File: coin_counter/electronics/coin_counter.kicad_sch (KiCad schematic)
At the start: 51 parts, among them J1 Q_EMT, J10 H_EMT, J11 Power In, J12 Q_BTN, J13 D_BTN, J14 N_BTN, J15 P_BTN, J16 UP_BTN, J17 DN_BTN, J18 VFD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

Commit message: fixed errors
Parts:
- removed R1, R2, R3, R4, R5, R6: 220 Ohm, Resistor_THT:R_Axial_DIN0204_L3.6mm_D1.6mm_P5.08mm_Vertical, symbol Device:R_US
- removed Sensor1: Mom, Connector_JST:JST_XH_B6B-XH-A_1x06_P2.50mm_Vertical, symbol Connector_Generic:Conn_02x03_Top_Bottom
- added R10, R11, R12, R7, R8, R9: 10k, Resistor_SMD:R_0201_0603Metric, symbol Device:R_US
- added Sensor2: Mom, Connector_JST:JST_XH_B6B-XH-A_1x06_P2.50mm_Vertical, symbol Connector_Generic:Conn_02x03_Top_Bottom
- C1, C2, C3: footprint Capacitor_THT:CP_Radial_D10.0mm_P5.00mm -> Capacitor_SMD:CP_Elec_5x5.9
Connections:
- net at A1.29 (GND), A1.4 (GND), H5.1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: no longer J11.1 (Pin_1), J22.1 (Pin_1)
- net at J15.1 (Pin_1): now also U1.3 (QD)
- net at J15.2 (Pin_2): now also R10.2; no longer U2.14 (D3)
- net at C1.2, C2.2, H10.1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: now also U2.5 (D6), U2.6 (D7), Sensor2.2 (Pin_2); no longer J12.3 (Pin_3), J13.3 (Pin_3), J14.3 (Pin_3), J15.3 (Pin_3), J16.3 (Pin_3), J17.3 (Pin_3)
- net at J19.2 (Pin_2), U2.1 (~{PL}): now also Sensor2.4 (Pin_4)
- net at U2.10 (DS): now also Sensor2.3 (Pin_3)
- net at U2.11 (D0): now also R7.1; no longer J12.2 (Pin_2)
- net at U2.12 (D1): now also R8.1; no longer J13.2 (Pin_2)
- net at U2.13 (D2): now also R9.1; no longer J14.2 (Pin_2)
- net at J19.4 (Pin_4), U2.15 (~{CE}): now also Sensor2.6 (Pin_6)
- net at C1.1, C2.1, J21.2 (Pin_2)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: now also J12.3 (Pin_3), J13.3 (Pin_3), J14.3 (Pin_3), J15.3 (Pin_3), J16.3 (Pin_3), J17.3 (Pin_3), Sensor2.1 (Pin_1)
- net at J19.3 (Pin_3), U2.2 (CP): now also Sensor2.5 (Pin_5)
- net at U2.3 (D4): now also R11.1; no longer J16.2 (Pin_2)
- net at U2.4 (D5): now also R12.1; no longer J17.2 (Pin_2)
- net at J5.3 (Pin_3): now also U3.9 (Q7); no longer U3.7 (~{Q7})
- net at U1.1 (QB): now also J13.1 (Pin_1)
- net at U1.15 (QA): now also J12.1 (Pin_1)
- net at U1.2 (QC): now also J14.1 (Pin_1)
- net at U1.4 (QE): now also J16.1 (Pin_1)
- net at U1.5 (QF): now also J17.1 (Pin_1)
- new net: J12.2 (Pin_2), R7.2
- new net: R10.1, U2.14 (D3)
- new net: J17.2 (Pin_2), R12.2
- new net: J16.2 (Pin_2), R11.2
- new net: J11.1 (Pin_1), J22.1 (Pin_1)
- new net: J13.2 (Pin_2), R8.2
- new net: J14.2 (Pin_2), R9.2

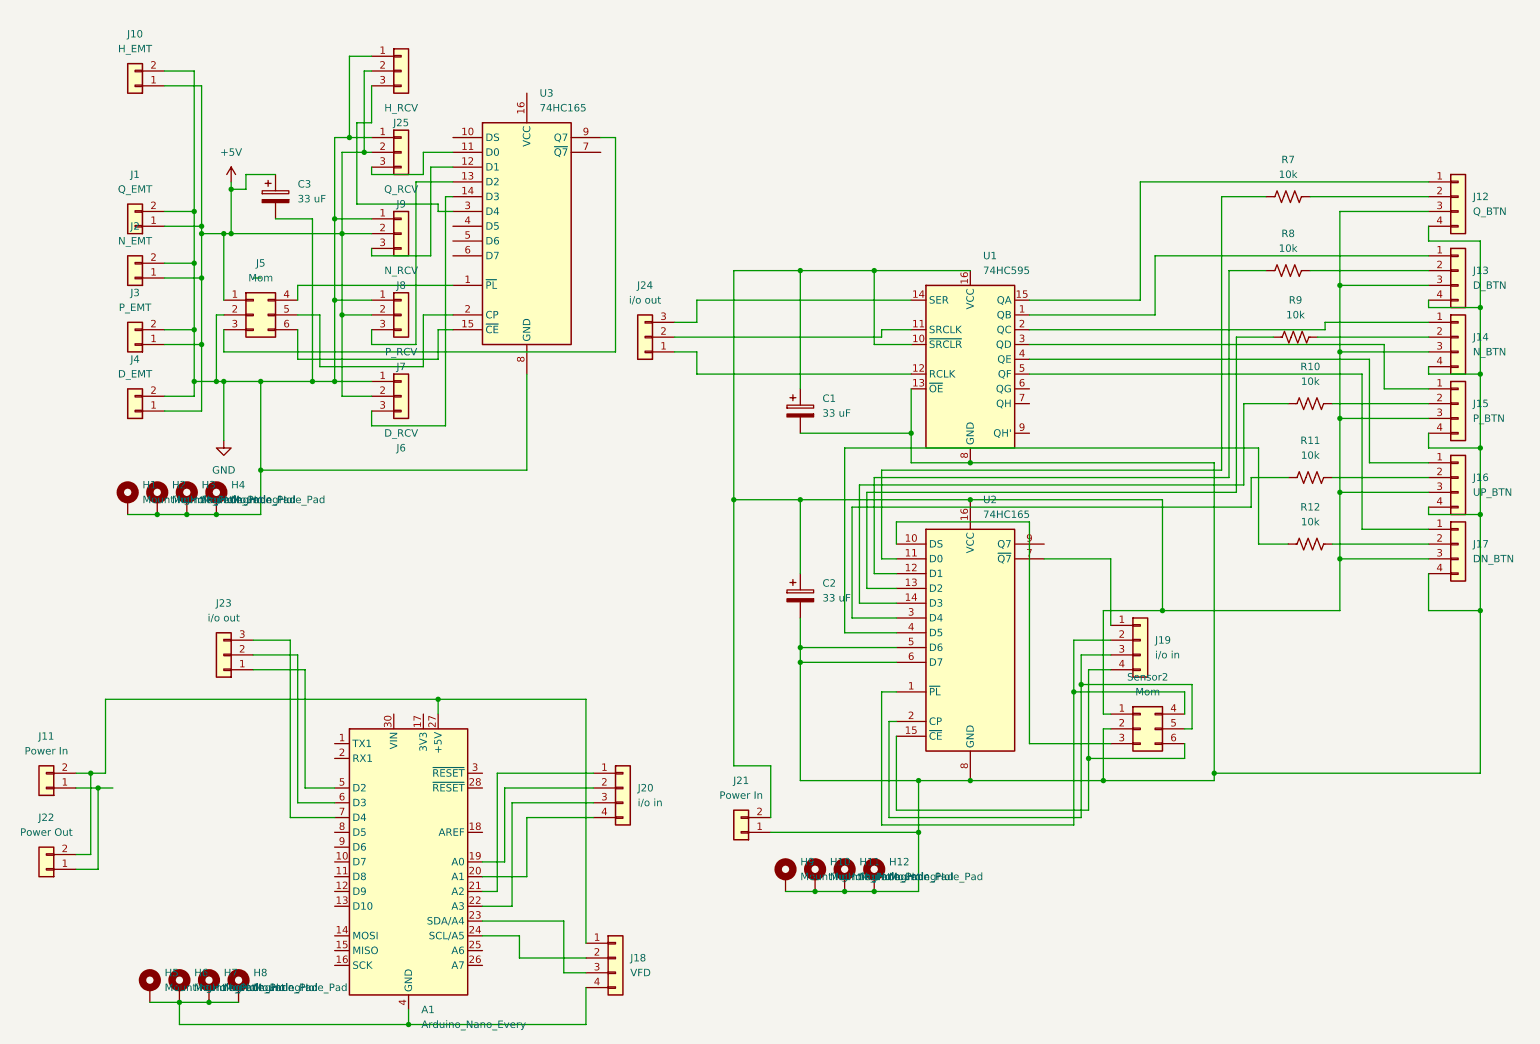
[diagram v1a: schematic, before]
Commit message: more work, mosfets and diodes
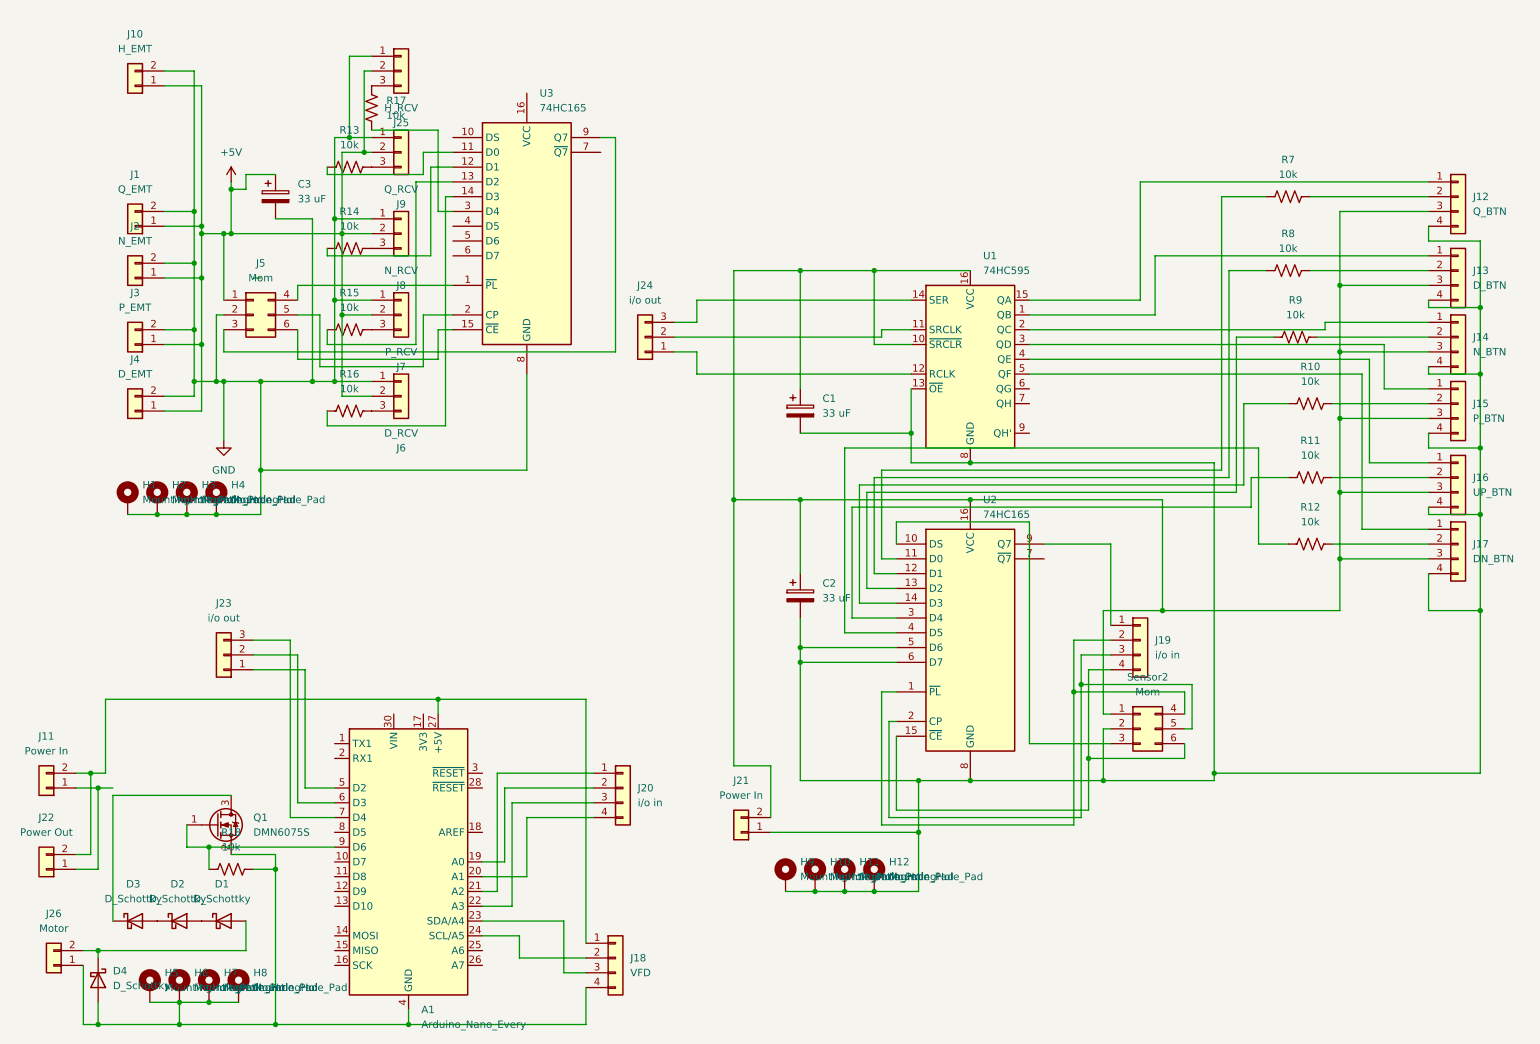
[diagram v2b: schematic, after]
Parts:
- added D1, D2, D3, D4: D_Schottky, Diode_SMD:D_SMA_Handsoldering, symbol Device:D_Schottky
- added J26: Motor, Connector_JST:JST_XH_B2B-XH-A_1x02_P2.50mm_Vertical, symbol Connector_Generic:Conn_01x02
- added Q1: DMN6075S, Package_TO_SOT_SMD:SOT-23, symbol Transistor_FET:DMN6075S
- added R13, R14, R15, R16, R17, R18: 10k, Resistor_SMD:R_0201_0603Metric, symbol Device:R_US
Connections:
- net at A1.29 (GND), A1.4 (GND), H5.1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: now also D4.2 (A), J26.1 (Pin_1), Q1.2 (S), R18.2
- net at U2.7 (~{Q7}): no longer J19.1 (Pin_1)
- net at U2.9 (Q7): now also J19.1 (Pin_1)
- net at J7.3 (Pin_3): now also R15.2; no longer U3.13 (D2)
- net at U3.11 (D0): now also R13.1; no longer J9.3 (Pin_3)
- net at U3.12 (D1): now also R14.1; no longer J8.3 (Pin_3)
- net at U3.14 (D3): now also R16.1; no longer J6.3 (Pin_3)
- net at U3.3 (D4): now also R17.1; no longer J25.3 (Pin_3)
- net at A1.9 (D6): now also Q1.1 (G), R18.1
- new net: D2.1 (K), D3.2 (A)
- new net: D1.1 (K), D2.2 (A)
- new net: J25.3 (Pin_3), R17.2
- new net: J9.3 (Pin_3), R13.2
- new net: R15.1, U3.13 (D2)
- new net: D1.2 (A), D4.1 (K), J26.2 (Pin_2)
- new net: J8.3 (Pin_3), R14.2
- new net: J6.3 (Pin_3), R16.2
- new net: D3.1 (K), Q1.3 (D)

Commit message: board layouts button and main
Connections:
- net at A1.29 (GND), A1.4 (GND), H5.1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: now also J11.1 (Pin_1), J22.1 (Pin_1); no longer D4.2 (A), J26.1 (Pin_1)
- net at A1.27 (+5V), J11.2 (Pin_2), J18.1 (Pin_1)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: now also D3.1 (K)
- net at Q1.3 (D): now also D4.2 (A), J26.1 (Pin_1); no longer D3.1 (K)
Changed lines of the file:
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@@
 	)
 	(junction
-		(at 49.53 152.4)
+		(at 30.48 179.07)
 		(diameter 0)
 		(color 0 0 0 0)
@@
 	)
 	(junction
-		(at 30.48 182.88)
-		(diameter 0)
-		(color 0 0 0 0)
-	)
-	(junction
 		(at 199.39 124.46)
 		(diameter 0)
@@
 	)
 	(junction
+		(at 45.72 148.59)
+		(diameter 0)
+		(color 0 0 0 0)
+	)
+	(junction
 		(at 198.12 125.73)
 		(diameter 0)
@@
 	)
 	(junction
-		(at 30.48 142.24)
-		(diameter 0)
-		(color 0 0 0 0)
-	)
-	(junction
 		(at 72.39 60.96)
 		(diameter 0)
@@
 	)
 	(junction
+		(at 31.75 139.7)
+		(diameter 0)
+		(color 0 0 0 0)
+	)
+	(junction
 		(at 29.21 139.7)
 		(diameter 0)
@@
 	)
 	(junction
+		(at 30.48 156.21)
+		(diameter 0)
+		(color 0 0 0 0)
+	)
+	(junction
 		(at 44.45 179.07)
 		(diameter 0)
@@
 	(wire
 		(pts
-			(xy 30.48 179.07) (xy 30.48 182.88)
-		)
-		(stroke
-			(width 0)
-			(type default)
-		)
-	)
-	(wire
-		(pts
 			(xy 96.52 162.56) (xy 101.6 162.56)
 		)
@@
 	(wire
 		(pts
+			(xy 19.05 158.75) (xy 30.48 158.75)
+		)
+		(stroke
+			(width 0)
+			(type default)
+		)
+	)
+	(wire
+		(pts
+			(xy 19.05 182.88) (xy 19.05 158.75)
+		)
+		(stroke
+			(width 0)
+			(type default)
+		)
+	)
+	(wire
+		(pts
 			(xy 88.9 29.21) (xy 77.47 29.21)
 		)
@@
 	(wire
 		(pts
-			(xy 69.85 80.01) (xy 90.17 80.01)
+			(xy 27.94 179.07) (xy 30.48 179.07)
 		)
 		(stroke
@@
 	(wire
 		(pts
-			(xy 170.18 58.42) (xy 133.35 58.42)
+			(xy 69.85 80.01) (xy 90.17 80.01)
 		)
 		(stroke
@@
 	(wire
 		(pts
-			(xy 110.49 173.99) (xy 110.49 165.1)
+			(xy 170.18 58.42) (xy 133.35 58.42)
 		)
 		(stroke
@@
 	(wire
 		(pts
-			(xy 27.94 172.72) (xy 27.94 182.88)
+			(xy 110.49 173.99) (xy 110.49 165.1)
 		)
 		(stroke
@@
 	(wire
 		(pts
+			(xy 30.48 158.75) (xy 30.48 156.21)
+		)
+		(stroke
+			(width 0)
+			(type default)
+		)
+	)
+	(wire
+		(pts
 			(xy 119.38 67.31) (xy 119.38 30.48)
 		)
@@
 	(wire
 		(pts
-			(xy 27.94 182.88) (xy 30.48 182.88)
+			(xy 170.18 73.66) (xy 170.18 81.28)
 		)
 		(stroke
@@
 	(wire
 		(pts
-			(xy 170.18 73.66) (xy 170.18 81.28)
+			(xy 165.1 102.87) (xy 165.1 87.63)
 		)
 		(stroke
@@
 	(wire
 		(pts
-			(xy 165.1 102.87) (xy 165.1 87.63)
+			(xy 71.12 152.4) (xy 57.15 152.4)
 		)
 		(stroke
@@
 	(wire
 		(pts
-			(xy 33.02 143.51) (xy 33.02 165.1)
+			(xy 33.02 139.7) (xy 33.02 165.1)
 		)
 		(stroke
@@
 	(wire
 		(pts
-			(xy 33.02 143.51) (xy 53.34 143.51)
-		)
-		(stroke
-			(width 0)
-			(type default)
-		)
-	)
-	(wire
-		(pts
 			(xy 100.33 142.24) (xy 115.57 142.24)
 		)
@@
 	(wire
 		(pts
+			(xy 38.1 143.51) (xy 38.1 179.07)
+		)
+		(stroke
+			(width 0)
+			(type default)
+		)
+	)
+	(wire
+		(pts
 			(xy 167.64 130.81) (xy 166.37 130.81)
 		)
@@
 	(wire
 		(pts
+			(xy 57.15 144.78) (xy 45.72 144.78)
+		)
+		(stroke
+			(width 0)
+			(type default)
+		)
+	)
+	(wire
+		(pts
 			(xy 41.91 52.07) (xy 46.99 52.07)
 		)
@@
 	(wire
 		(pts
+			(xy 38.1 179.07) (xy 30.48 179.07)
+		)
+		(stroke
+			(width 0)
+			(type default)
+		)
+	)
+	(wire
+		(pts
 			(xy 60.96 44.45) (xy 67.31 44.45)
 		)
@@
 	(wire
 		(pts
-			(xy 203.2 111.76) (xy 213.36 111.76)
+			(xy 27.94 172.72) (xy 27.94 179.07)
 		)
 		(stroke
@@
 	(wire
 		(pts
-			(xy 48.26 54.61) (xy 48.26 46.99)
+			(xy 203.2 111.76) (xy 213.36 111.76)
 		)
 		(stroke
@@
 	(wire
 		(pts
-			(xy 57.15 54.61) (xy 58.42 54.61)
+			(xy 48.26 54.61) (xy 48.26 46.99)
 		)
 		(stroke
@@
 	(wire
 		(pts
-			(xy 165.1 64.77) (xy 165.1 63.5)
+			(xy 57.15 54.61) (xy 58.42 54.61)
 		)
 		(stroke
@@
 	(wire
 		(pts
-			(xy 167.64 146.05) (xy 200.66 146.05)
+			(xy 165.1 64.77) (xy 165.1 63.5)
 		)
 		(stroke
@@
 	(wire
 		(pts
-			(xy 259.08 93.98) (xy 259.08 95.25)
+			(xy 167.64 146.05) (xy 200.66 146.05)
 		)
 		(stroke
@@
 	(wire
 		(pts
-			(xy 151.13 120.65) (xy 167.64 120.65)
+			(xy 259.08 93.98) (xy 259.08 95.25)
 		)
 		(stroke
@@
 	(wire
 		(pts
-			(xy 49.53 152.4) (xy 71.12 152.4)
+			(xy 151.13 120.65) (xy 167.64 120.65)
 		)
 		(stroke
@@
 	(wire
 		(pts
-			(xy 30.48 142.24) (xy 33.02 142.24)
-		)
-		(stroke
-			(width 0)
-			(type default)
-		)
-	)
-	(wire
-		(pts
 			(xy 160.02 93.98) (xy 160.02 113.03)
 		)
@@
 	(wire
 		(pts
+			(xy 57.15 152.4) (xy 57.15 144.78)
+		)
+		(stroke
+			(width 0)
+			(type default)
+		)
+	)
+	(wire
+		(pts
 			(xy 69.85 50.8) (xy 69.85 49.53)
 		)
@@
 	(wire
 		(pts
+			(xy 53.34 143.51) (xy 38.1 143.51)
+		)
+		(stroke
+			(width 0)
+			(type default)
+		)
+	)
+	(wire
+		(pts
 			(xy 198.12 116.84) (xy 204.47 116.84)
 		)
@@
 	(wire
 		(pts
+			(xy 45.72 144.78) (xy 45.72 148.59)
+		)
+		(stroke
+			(width 0)
+			(type default)
+		)
+	)
+	(wire
+		(pts
+			(xy 33.02 139.7) (xy 31.75 139.7)
+		)
+		(stroke
+			(width 0)
+			(type default)
+		)
+	)
+	(wire
+		(pts
 			(xy 251.46 73.66) (xy 251.46 66.04)
 		)
@@
 	(wire
 		(pts
-			(xy 30.48 182.88) (xy 44.45 182.88)
+			(xy 19.05 182.88) (xy 44.45 182.88)
 		)
 		(stroke

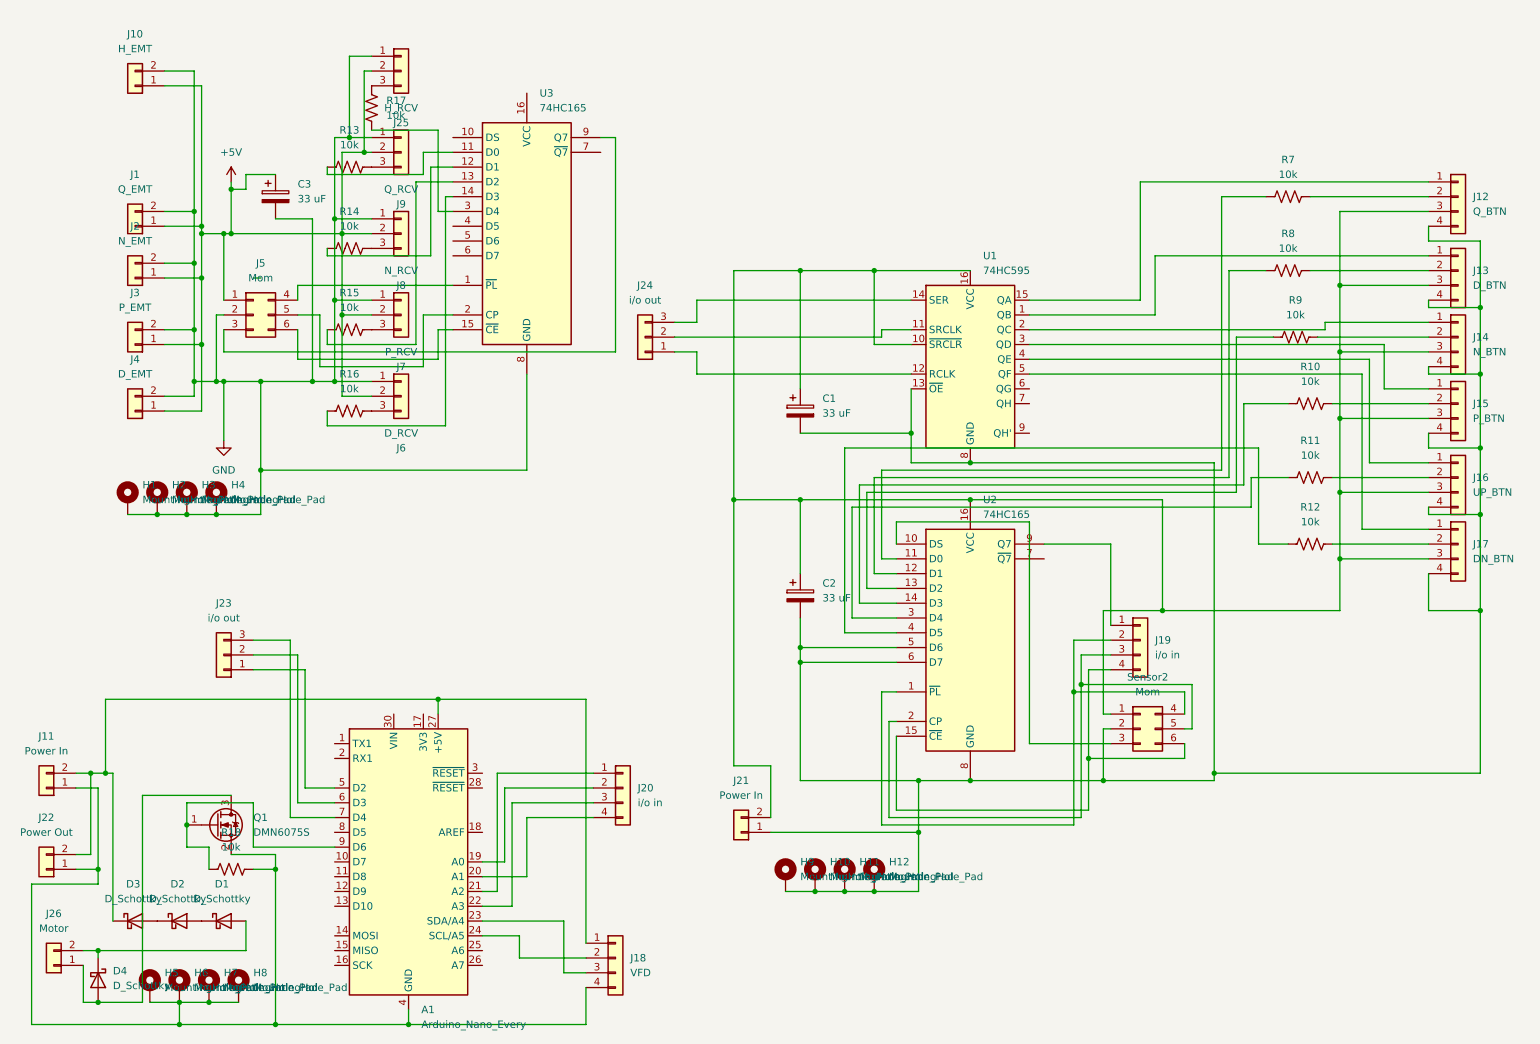
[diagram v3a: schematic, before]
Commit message: only take the VFD stuff I need
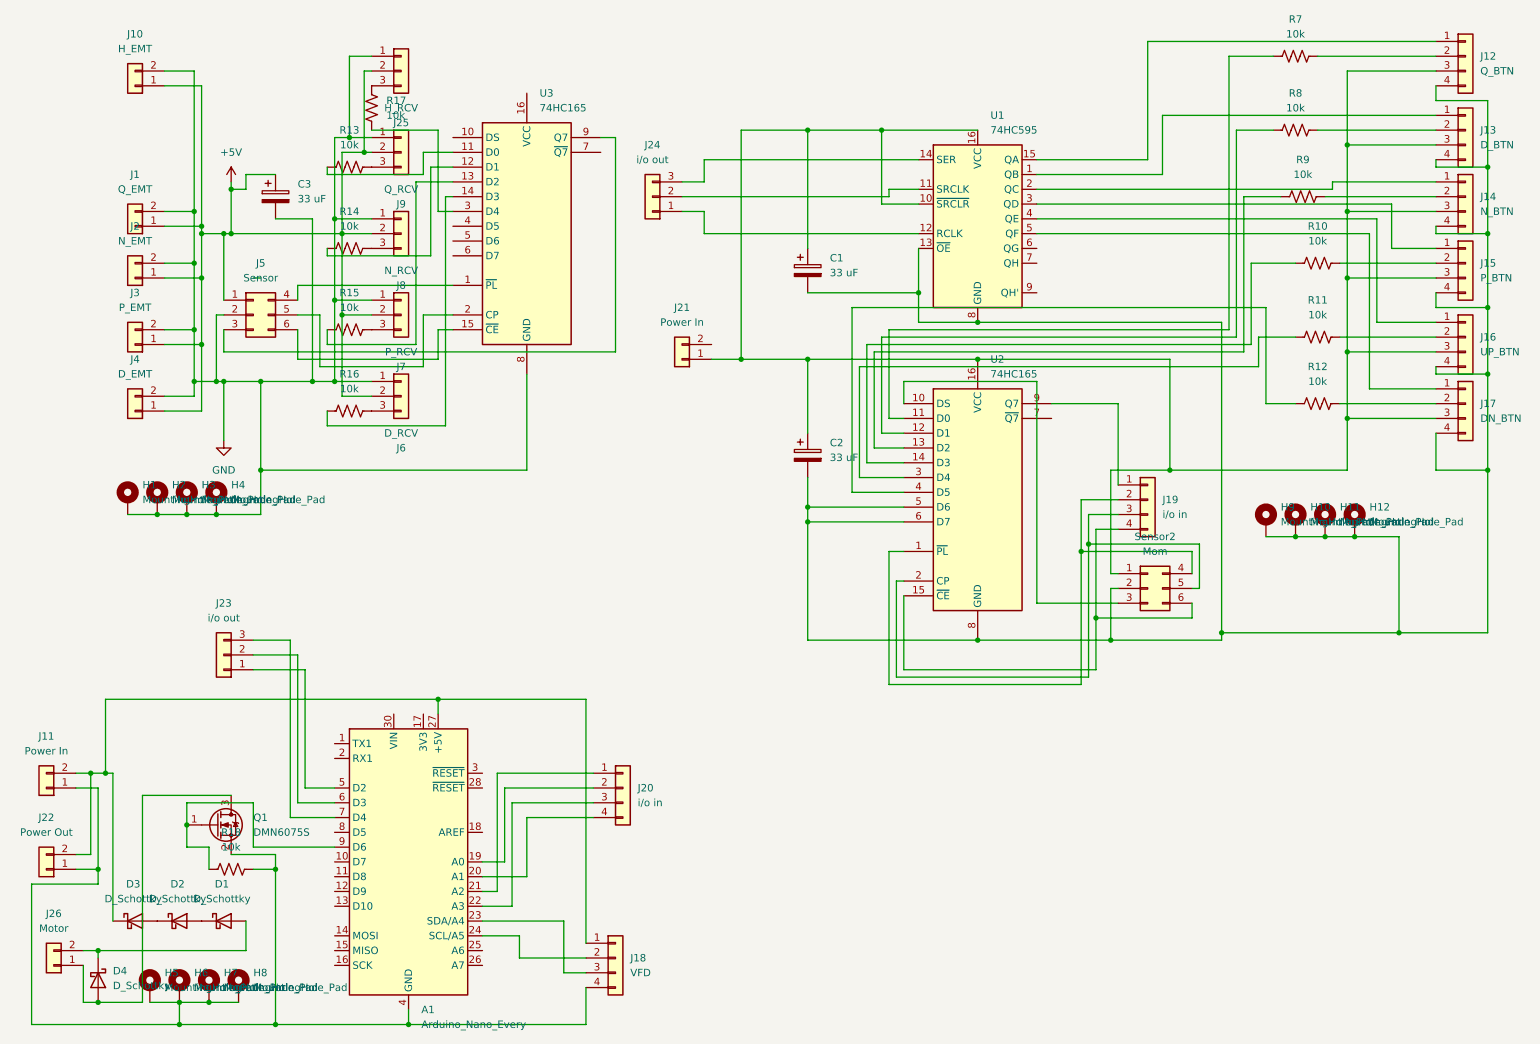
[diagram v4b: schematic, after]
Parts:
- J5: value Mom -> Sensor
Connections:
- net at C1.1, C2.1, J12.3 (Pin_3)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: now also J21.1 (Pin_1); no longer J21.2 (Pin_2)
- net at C1.2, C2.2, H10.1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: no longer J21.1 (Pin_1)
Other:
- moved on the sheet: C1, C2, H10, H11, H12, H9, J12, J13, J14, J15, J16, J17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
